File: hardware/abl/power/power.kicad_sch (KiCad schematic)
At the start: 30 parts, among them J1 Terminal_01x03, J2 Terminal_01x03, J3 009159008603906, U1 TWGMC AMS1117-3.3, U2 TMP1075D, U3 INA219AxD

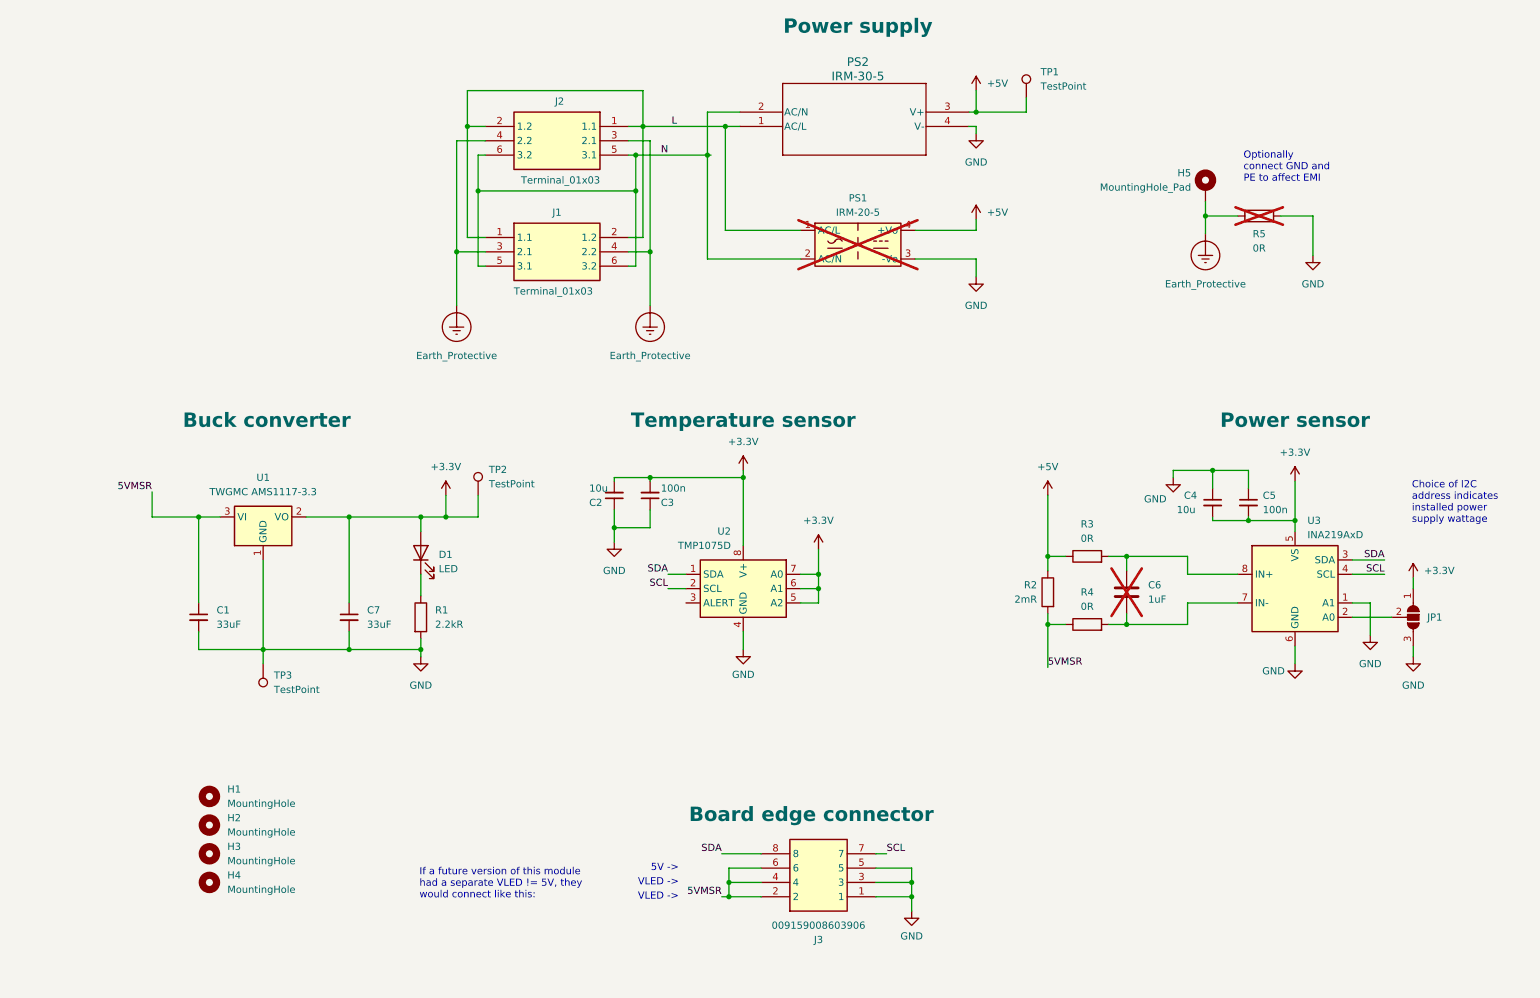
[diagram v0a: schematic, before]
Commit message: Add own / optimized footprints (bigger pads), add fuse and current limiting to the power module.
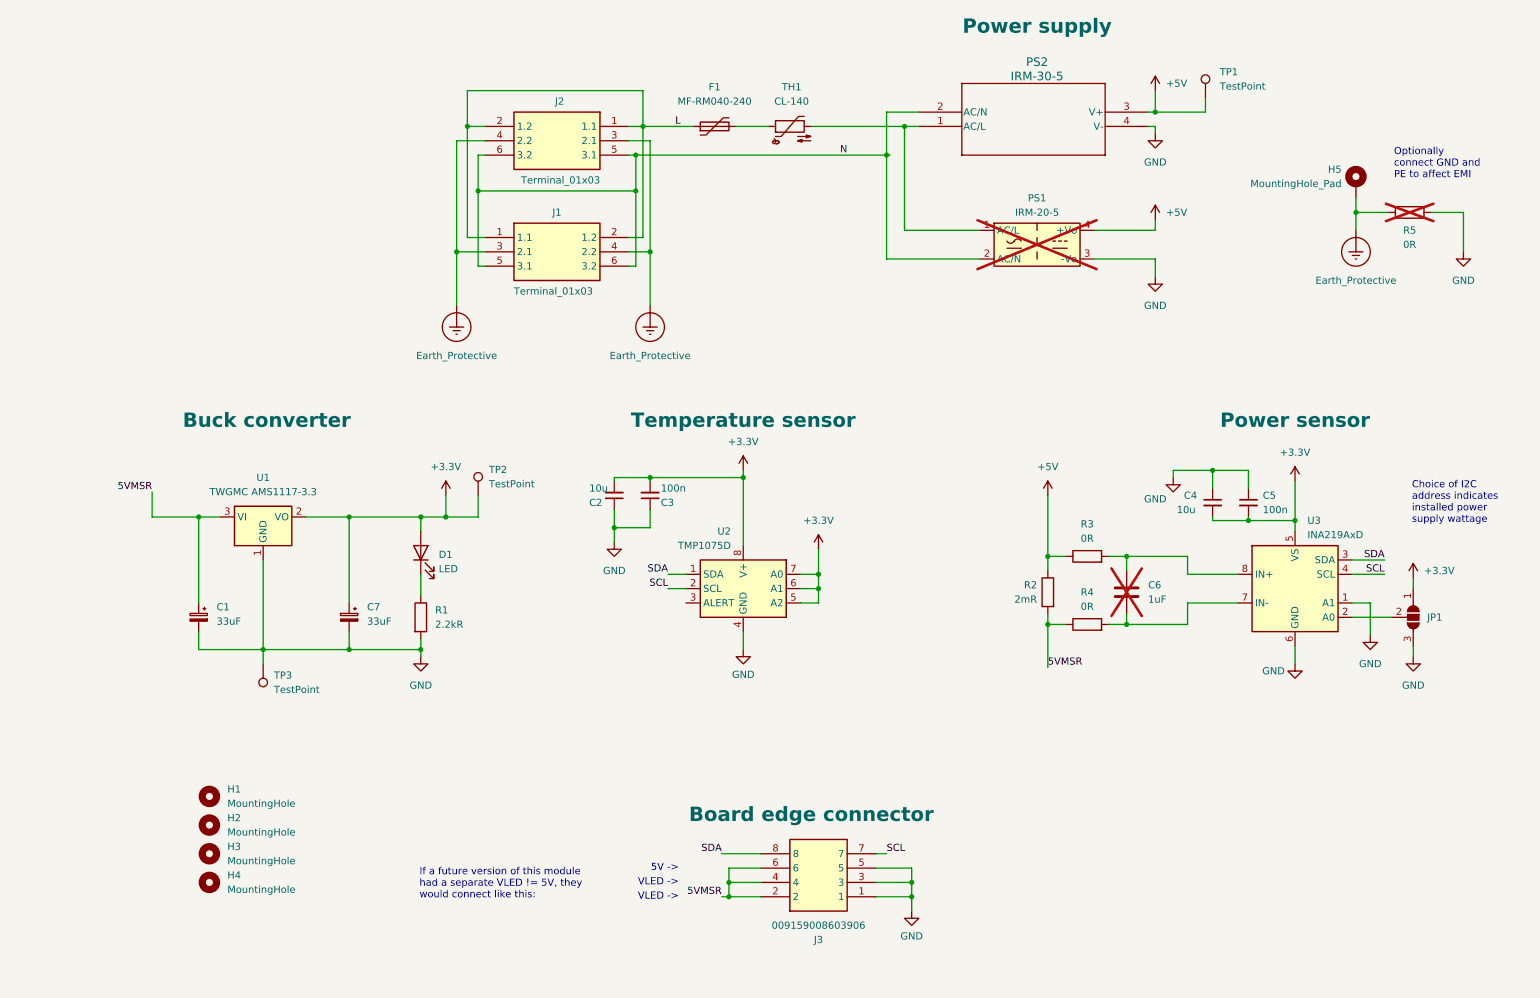
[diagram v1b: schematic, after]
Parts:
- added F1: MF-RM040-240, Own footprints:Bourns MF-RM055-240 resettable fuse, symbol Device:Polyfuse
- added TH1: CL-140, Own footprints:Amphenol NTC Inrush Current Limiter CL-140, symbol Device:Thermistor_NTC
- C1, C7: symbol Device:C_Small -> Device:C_Polarized_Small
- J1, J2: footprint WAGO-2604-1103:26041103 -> Own footprints:WAGO-2604-1103
- PS2: footprint IRM-30_MWU -> Own footprints:Converter_ACDC_MeanWell_IRM-20+30-xx_THT_combined
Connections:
- net L: now also F1.1; no longer PS1.1 (AC/L), PS2.1 (AC/L)
- new net: F1.2, TH1.1
- new net: PS1.1 (AC/L), PS2.1 (AC/L), TH1.2
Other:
- moved on the sheet: H5, PS1, PS2, R5, TP1

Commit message: A few smaller updates to some PCBs and their READMEs.
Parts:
- C1, C7: LCSC Part C308920 -> C7203; Manufacturer_Part_Number TPSB336M016R0350 -> TAJB336K016RNJ
- D1: footprint LED_THT:LED_D3.0mm_Horizontal_O3.81mm_Z10.0mm -> Own footprints:XINGLIGHT XL-3210SURC; LCSC Part (none) -> C965874; Manufacturer_Part_Number (none) -> XL-3210SURC; Purpose (none) -> Power LED
- F1: Purpose (none) -> Fuse
- J1, J2: Purpose (none) -> 230V connector
- J3: footprint 009159008603906 -> Own footprints:Dual Row Inverted Thru Board Card Edge Connector 02x04 Kyocera AVX 009159008603906
- TH1: Purpose (none) -> Inrush current limiter
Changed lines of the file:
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@@
 			)
 		)
+		(property "Purpose" "Fuse"
+			(at 135.255 44.45 0)
+			(effects
+				(font
+					(size 1.27 1.27)
+				)
+				(hide yes)
+			)
+		)
 		(pin "2"
 		)
@@
 			)
 		)
-		(property "LCSC Part" "C308920"
+		(property "LCSC Part" "C7203"
 			(at 43.815 131.445 0)
 			(effects
@@
 			)
 		)
-		(property "Manufacturer_Part_Number" "TPSB336M016R0350"
+		(property "Manufacturer_Part_Number" "TAJB336K016RNJ"
 			(at 43.815 131.445 0)
 			(effects
@@
 			)
 		)
-		(property "LCSC Part" "C308920"
+		(property "LCSC Part" "C7203"
 			(at 70.485 131.445 0)
 			(effects
@@
 			)
 		)
-		(property "Manufacturer_Part_Number" "TPSB336M016R0350"
+		(property "Manufacturer_Part_Number" "TAJB336K016RNJ"
 			(at 70.485 131.445 0)
 			(effects
@@
 			)
 		)
+		(property "Purpose" "Inrush current limiter"
+			(at 148.59 44.45 0)
+			(effects
+				(font
+					(size 1.27 1.27)
+				)
+				(hide yes)
+			)
+		)
 		(pin "2"
 		)
@@
 			)
 		)
-		(property "Purpose" ""
+		(property "Purpose" "230V connector"
 			(at 94.615 64.135 0)
 			(effects
@@
 			)
 		)
-		(property "Purpose" ""
+		(property "Purpose" "230V connector"
 			(at 120.015 44.45 0)
 			(effects
@@
 			)
 		)
-		(property "Footprint" "009159008603906"
+		(property "Footprint" "Own footprints:Dual Row Inverted Thru Board Card Edge Connector 02x04 Kyocera AVX 009159008603906"
 			(at 160.02 86.055 0)
 			(effects
@@
 			)
 		)
-		(property "Footprint" "LED_THT:LED_D3.0mm_Horizontal_O3.81mm_Z10.0mm"
+		(property "Footprint" "Own footprints:XINGLIGHT XL-3210SURC"
 			(at 83.185 120.015 0)
 			(effects
@@
 			)
 		)
-		(property "Purpose" ""
+		(property "Purpose" "Power LED"
+			(at 83.185 120.015 0)
+			(effects
+				(font
+					(size 1.27 1.27)
+				)
+				(hide yes)
+			)
+		)
+		(property "LCSC Part" "C965874"
+			(at 83.185 120.015 0)
+			(effects
+				(font
+					(size 1.27 1.27)
+				)
+				(hide yes)
+			)
+		)
+		(property "Manufacturer_Part_Number" "XL-3210SURC"
 			(at 83.185 120.015 0)
 			(effects

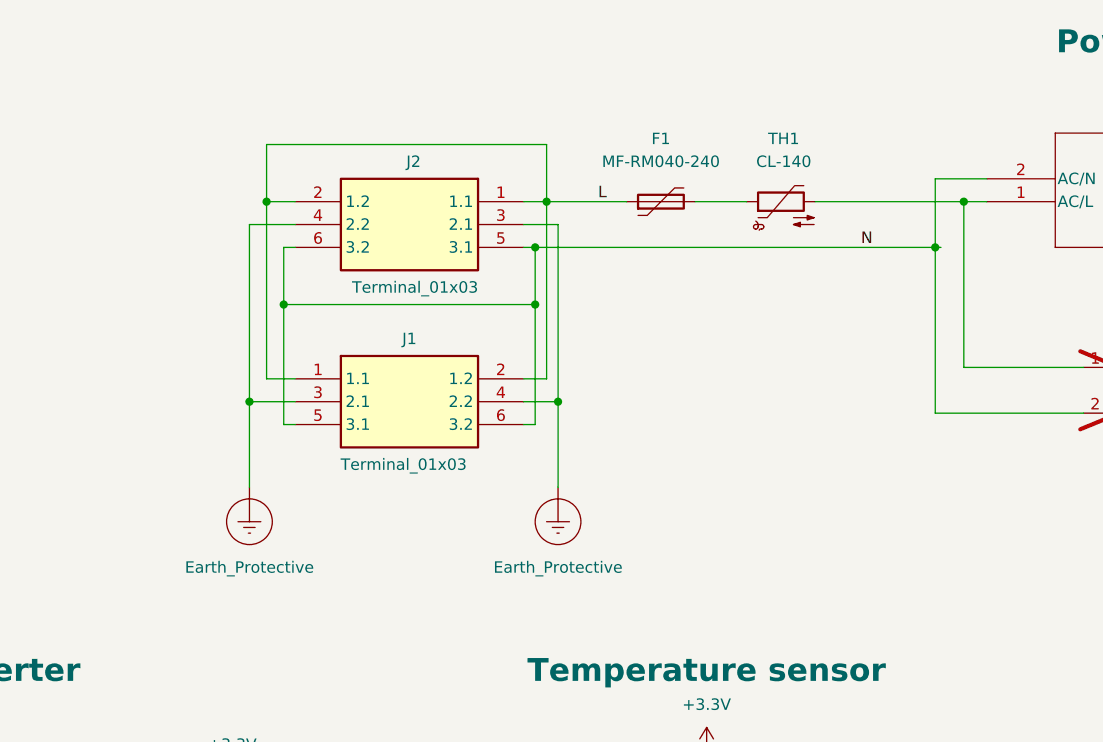
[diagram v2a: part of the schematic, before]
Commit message: Increase clearance of 230V nets to 3.175 mm, the maximum that is attainable with WAGO connerctors anyway.
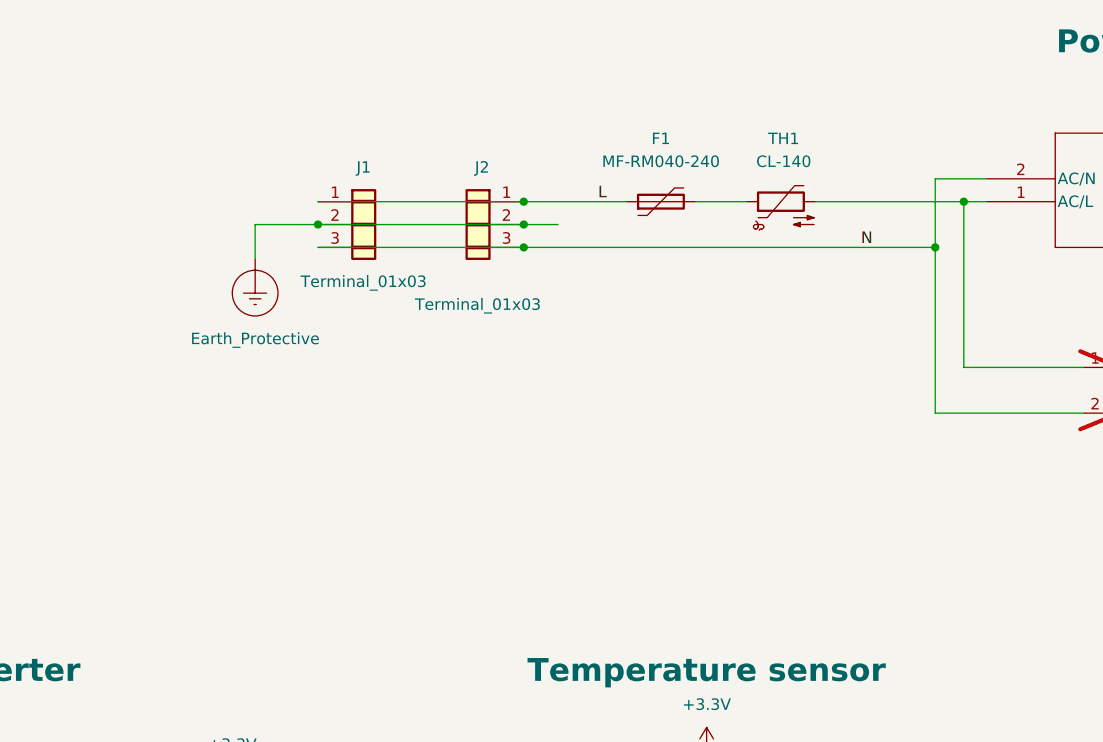
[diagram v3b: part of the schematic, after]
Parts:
- J1, J2: symbol WAGO-2604-1103:2604-1103 -> Connector_Generic:Conn_01x03_thru
- R5: footprint Resistor_SMD:R_0805_2012Metric -> Resistor_SMD:R_1206_3216Metric
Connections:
- net Earth_Protective: now also J1.2 (Pin_2), J2.2 (Pin_2); no longer J1.3 (2.1), J1.4 (2.2), J2.3 (2.1), J2.4 (2.2)
- net L: no longer J1.2 (1.2), J2.2 (1.2)
- net N: now also J1.3 (Pin_3), J2.3 (Pin_3); no longer J1.5 (3.1), J1.6 (3.2), J2.5 (3.1), J2.6 (3.2)

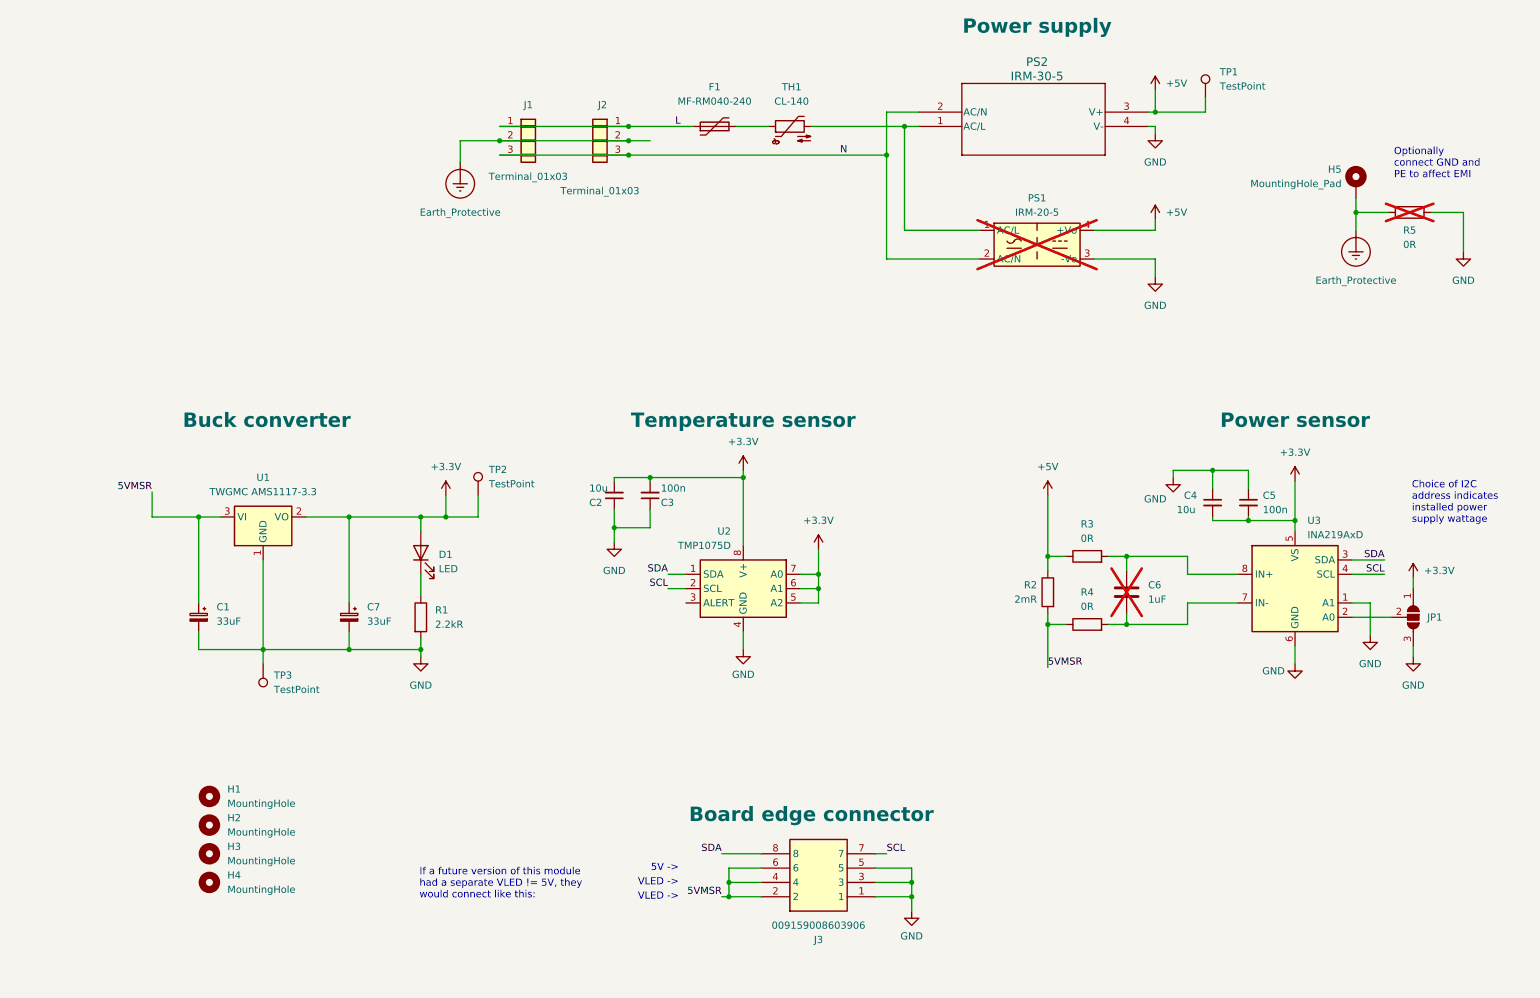
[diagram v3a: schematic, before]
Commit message: Added an EEPROM to the power module and changed the EEPROM on the LED module to be individually addressable.
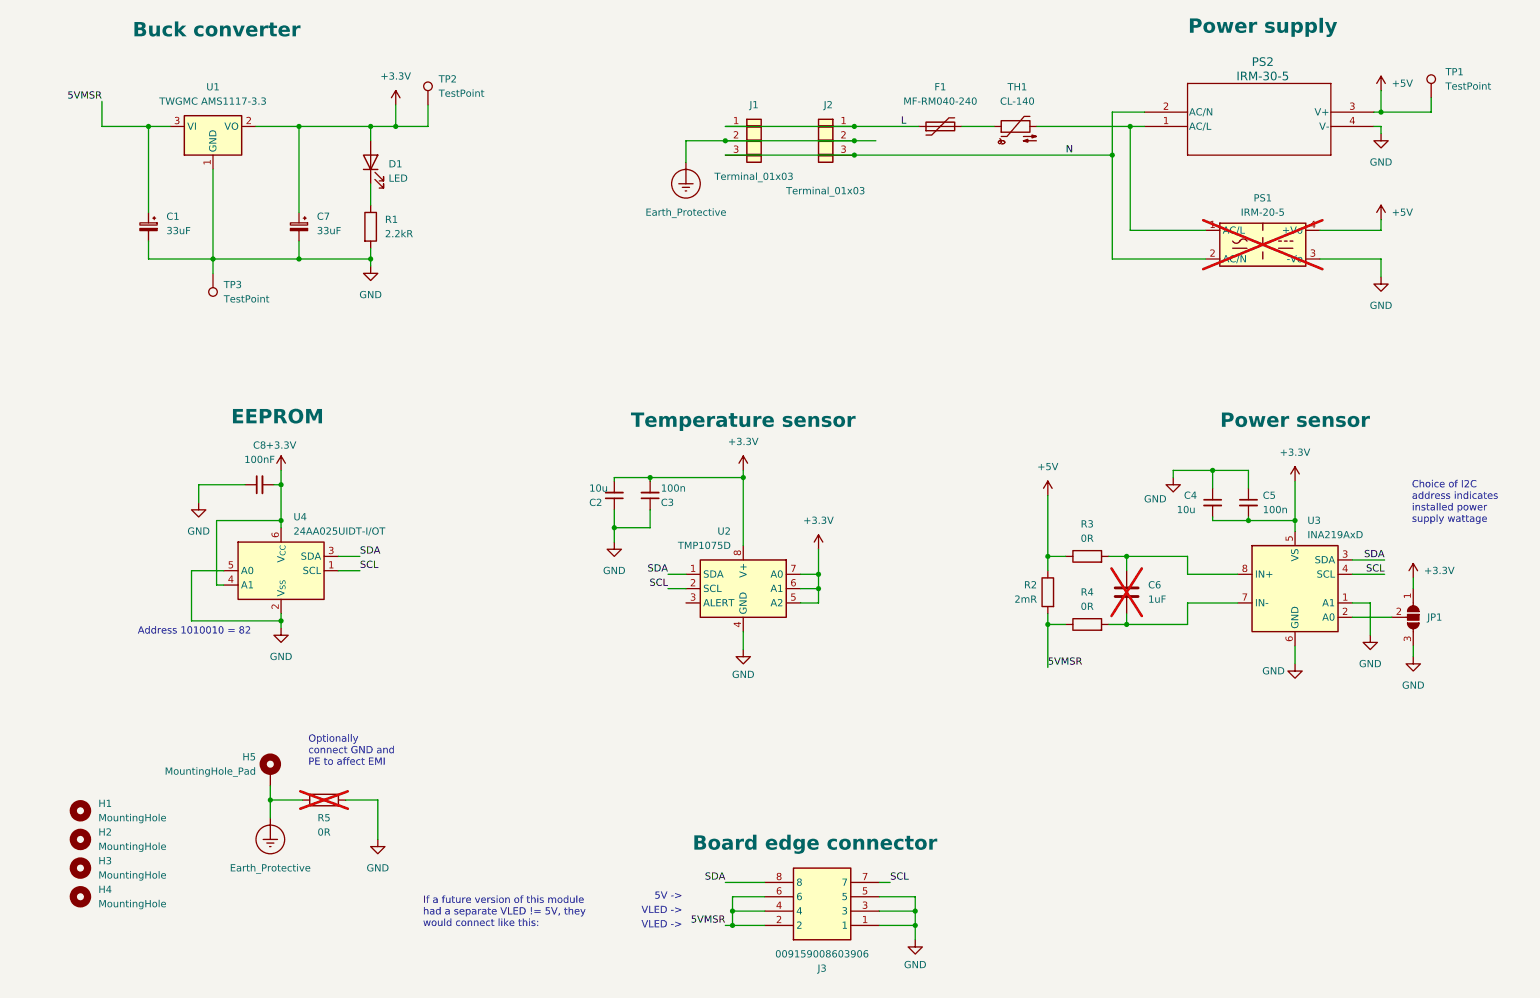
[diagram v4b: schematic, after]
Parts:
- added C8: 100nF, Capacitor_SMD:C_0402_1005Metric, symbol Device:C_Small
- added U4: 24AA025UIDT-I/OT, Package_TO_SOT_SMD:SOT-23-6, symbol Memory_EEPROM:24AA02XEXX
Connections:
- net +3.3V: now also C8.2, U4.4 (A1), U4.6 (V_{CC})
- net GND: now also C8.1, U4.2 (V_{SS}), U4.5 (A0)
- net SCL: now also U4.1 (SCL)
- net SDA: now also U4.3 (SDA)
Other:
- note added: "Address 1010010 = 82"
- moved on the sheet: C1, C7, D1, F1, H1, H2, H3, H4, H5, J1, J2, J3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
